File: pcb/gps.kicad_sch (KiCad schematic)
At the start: 7 parts, among them J10 RF_SMA, U18 MAX-M10S

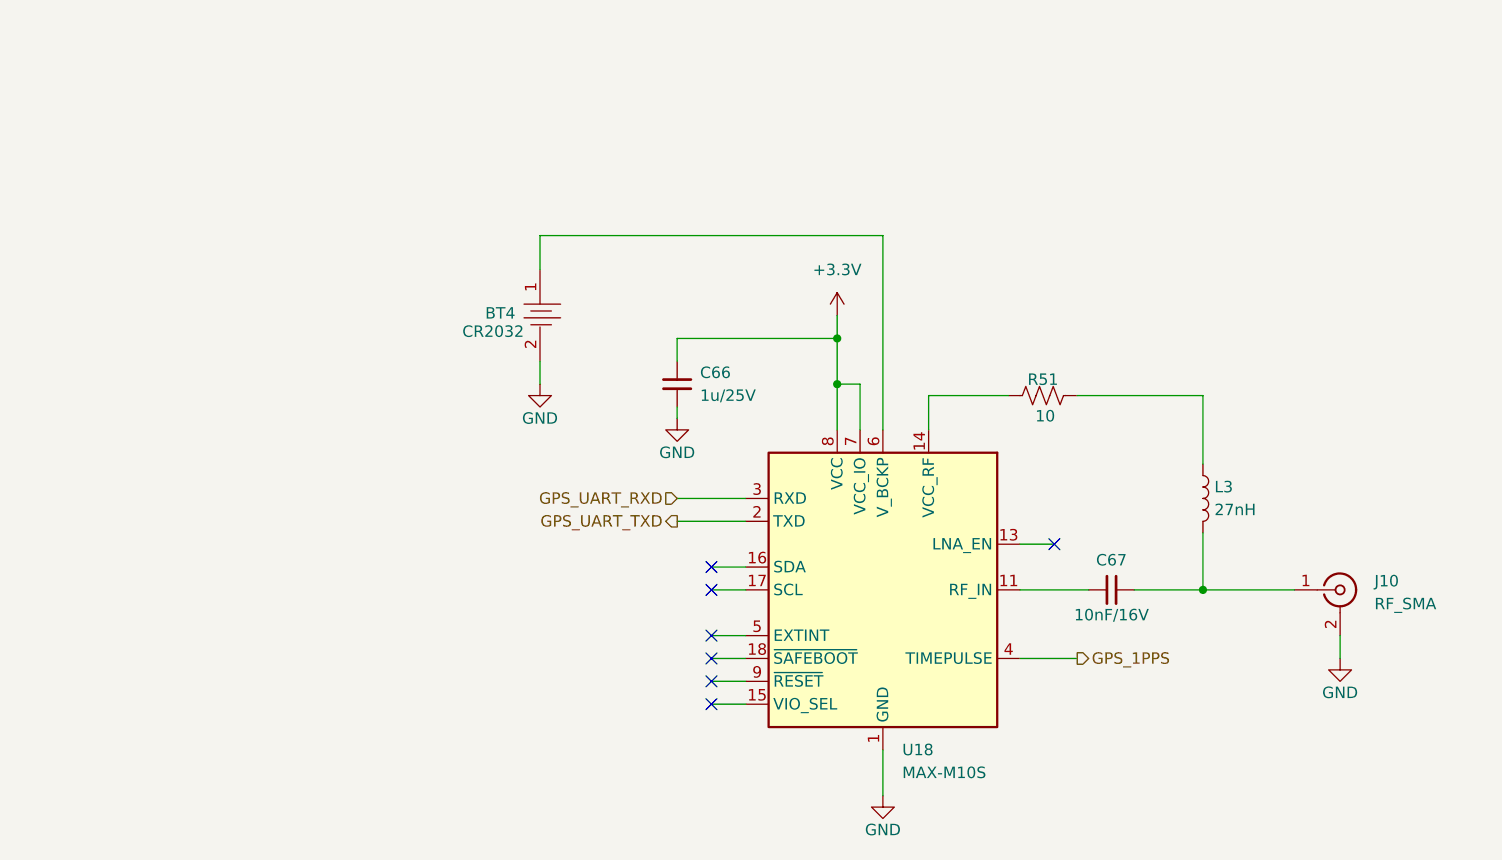
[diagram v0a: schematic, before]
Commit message: Wire GPS backup power network, import 4-layer stackup, add RF netclass
- gps.kicad_sch: CR2032/supercap backup network for V_BCKP (D6/D11/D12
  BAS116LT1G diodes, R52 10R charge resistor, C68 EDC474Z5R5V
  supercap), net labels GPS_RF_ANT/GPS_RF_IN on the antenna trace.
- foxhunt1.kicad_pcb: real JLCPCB 4-layer 1.6mm stackup imported
  (outer1oz/inner0.5oz, JLC04161H-7628/NOREQ construction).
- foxhunt1.kicad_pro: GPS_RF_50R netclass (2.75mm, sized for the prior
  2-layer board — needs updating to ~0.35mm once the 4-layer ground
  plane assignment is confirmed).

Co-Authored-By: Claude Sonnet 5 <noreply@anthropic.com>
Claude-Session: https://claude.ai/code/session_01LhLkuH6sQ5GbUZ61bG7p2h
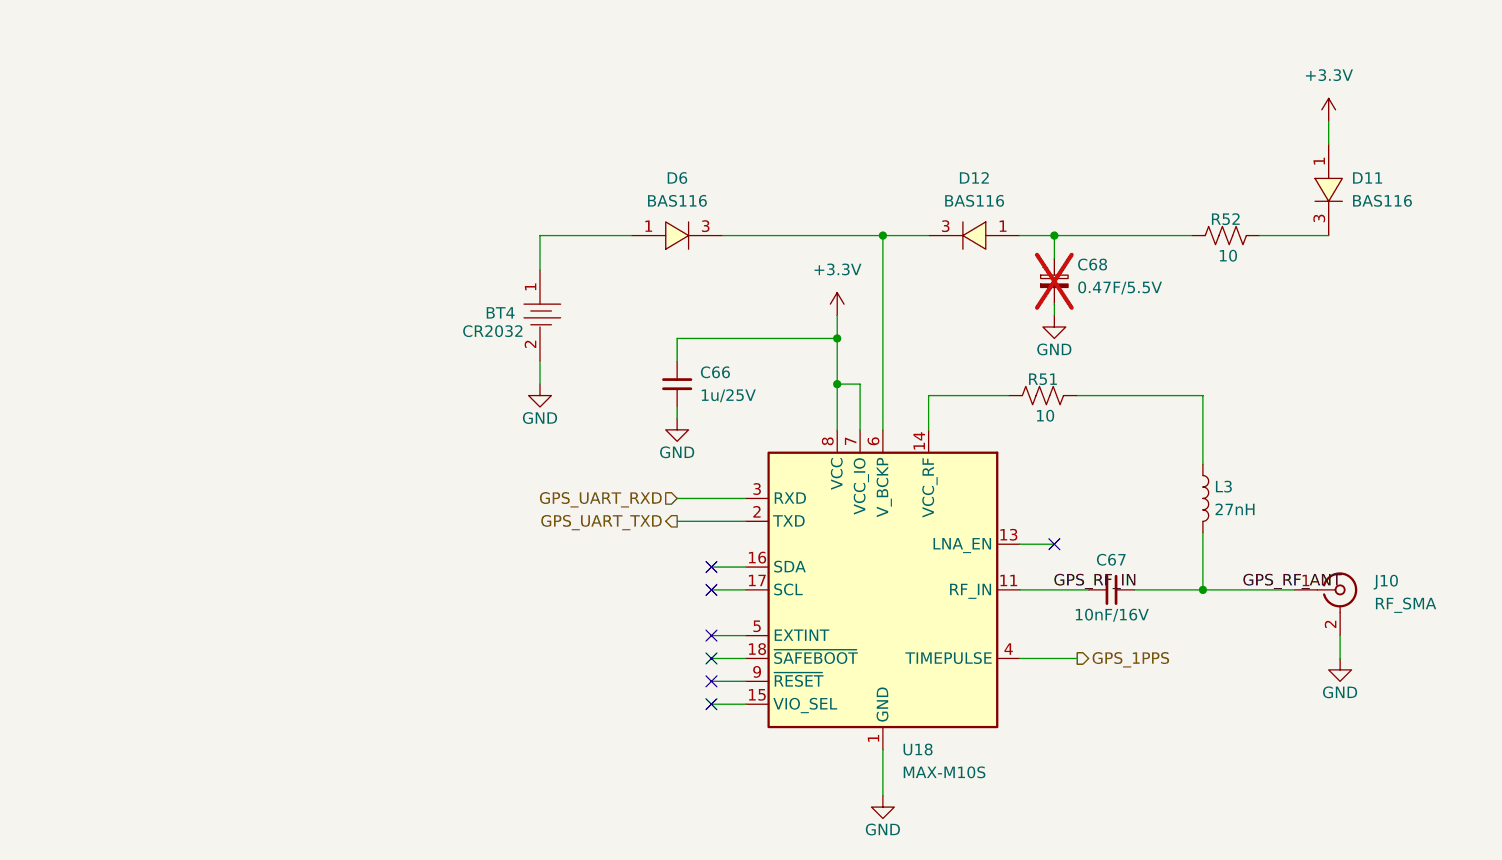
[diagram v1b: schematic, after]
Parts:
- added C68: 0.47F/5.5V, kicad_gx_library:CP_Supercap_EDC474Z5R5V_0.2x5mm, symbol Device:C_Polarized_Small
- added D11, D12, D6: BAS116, kicad_gx_library:SOT-23_L2.9-W1.3-P1.90-LS2.4-BR, symbol kicad_gx_library:BAS116LT1G
- added R52: 10, Resistor_SMD:R_0603_1608Metric, symbol Device:R_US
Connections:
- net +3.3V: now also D11.1
- net GND: now also C68.2
- net GPS_RF_IN: now reaches C67.1, U18.11 (RF_IN)
- net at U18.6 (V_BCKP): now also D12.3, D6.3; no longer BT4.1
- net GPS_RF_ANT: now reaches C67.2, J10.1 (In), L3.2
- new net: C68.1, D12.1, R52.2
- new net: BT4.1, D6.1
- new net: D11.3, R52.1

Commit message: Add SA818S-V sheet, update GPS antenna connector, MCU GPIO reassignments
- New SA818S-V sheet (U19): UART/PTT/MIC_IN wired; VBAT, ANT, PD, H/L
  still open (see sa818_pinout.md).
- gps.kicad_sch: J10 swapped to Amphenol 132289 edge-launch SMD SMA
  (same part planned for the SA818 antenna connector).
- mcu-esp32.kicad_sch: SA818 UART on IO6/IO7, PTT on IO16 (direct FET
  drive via Q10, not the originally-planned AND-gate scheme).
- peripherals.kicad_sch: in-progress PCA9555 channel changes.

Co-Authored-By: Claude Sonnet 5 <noreply@anthropic.com>
Claude-Session: https://claude.ai/code/session_01LhLkuH6sQ5GbUZ61bG7p2h
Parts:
- J10: footprint Connector_Coaxial:SMA_Amphenol_132134_Vertical -> Connector_Coaxial:SMA_Amphenol_132289_EdgeMount; LCSC Part # C3174425 -> C3172723; MPN 132134 -> 132289
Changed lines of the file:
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@@
 	(paper "A4")
+	(junction
+		(at 137.16 49.53)
+		(diameter 0)
+		(color 0 0 0 0)
+	)
 	(junction
 		(at 181.61 88.9)
@@
 	(wire
 		(pts
-			(xy 146.05 49.53) (xy 128.27 49.53)
+			(xy 146.05 49.53) (xy 137.16 49.53)
 		)
 		(stroke
@@
 		(pts
 			(xy 195.58 36.83) (xy 195.58 39.37)
+		)
+		(stroke
+			(width 0)
+			(type default)
+		)
+	)
+	(wire
+		(pts
+			(xy 137.16 49.53) (xy 128.27 49.53)
 		)
 		(stroke
@@
 	)
 	(symbol
+		(lib_id "power:PWR_FLAG")
+		(at 137.16 49.53 0)
+		(unit 1)
+		(body_style 1)
+		(exclude_from_sim no)
+		(in_bom yes)
+		(on_board yes)
+		(in_pos_files yes)
+		(dnp no)
+		(fields_autoplaced yes)
+		(property "Reference" "#FLG022"
+			(at 137.16 47.625 0)
+			(hide yes)
+			(show_name no)
+			(do_not_autoplace no)
+			(effects
+				(font
+					(size 1.27 1.27)
+				)
+			)
+		)
+		(property "Value" "PWR_FLAG"
+			(at 137.16 44.45 0)
+			(show_name no)
+			(do_not_autoplace no)
+			(effects
+				(font
+					(size 1.27 1.27)
+				)
+			)
+		)
+		(property "Footprint" ""
+			(at 137.16 49.53 0)
+			(hide yes)
+			(show_name no)
+			(do_not_autoplace no)
+			(effects
+				(font
+					(size 1.27 1.27)
+				)
+			)
+		)
+		(property "Datasheet" ""
+			(at 137.16 49.53 0)
+			(hide yes)
+			(show_name no)
+			(do_not_autoplace no)
+			(effects
+				(font
+					(size 1.27 1.27)
+				)
+			)
+		)
+		(property "Description" "Special symbol for telling ERC where power comes from"
+			(at 137.16 49.53 0)
+			(hide yes)
+			(show_name no)
+			(do_not_autoplace no)
+			(effects
+				(font
+					(size 1.27 1.27)
+				)
+			)
+		)
+		(pin "1"
+		)
+		(instances
+			(project "foxhunt1"
+				(path "/8399ba4b-9428-480d-8b65-76cf154b97a5/0c171942-64eb-4f5d-b37e-356ed65ec40c"
+					(reference "#FLG022")
+					(unit 1)
+				)
+			)
+		)
+	)
+	(symbol
 		(lib_id "kicad_gx_library:BAS116LT1G")
 		(at 156.21 49.53 180)
@@
 			)
 		)
-		(property "Footprint" "Connector_Coaxial:SMA_Amphenol_132134_Vertical"
+		(property "Footprint" "Connector_Coaxial:SMA_Amphenol_132289_EdgeMount"
 			(at 196.85 88.9 0)
 			(hide yes)
@@
 			)
 		)
-		(property "MPN" "132134"
+		(property "MPN" "132289"
 			(at 196.85 88.9 0)
 			(hide yes)
@@
 			)
 		)
-		(property "LCSC Part #" "C3174425"
+		(property "LCSC Part #" "C3172723"
 			(at 196.85 88.9 0)
 			(hide yes)

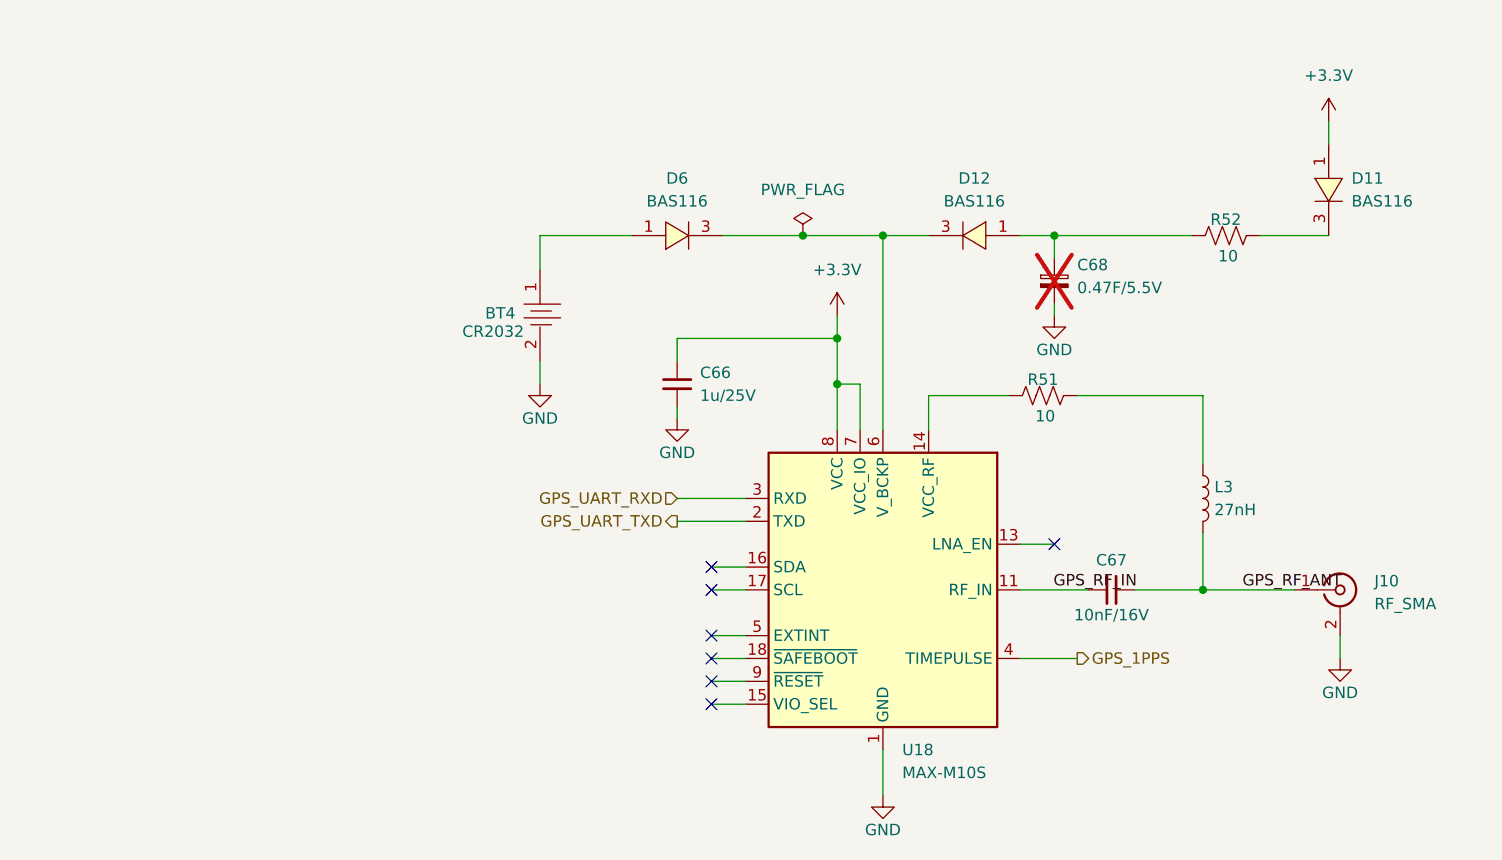
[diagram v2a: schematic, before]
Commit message: Wire SA818 PD/H-L and PTT opto, GPS power gating with bench bypass, RF detector groundwork
- SA818S-V: wire PD/H-L to PCA9555 expander outputs; swap PTT-keying FET
  for PC817 optocoupler isolation on the shared SA818S/external-HT PTT line
- GPS: add Q10 (AO3407A) high-side P-FET gating VCC+VCC_IO together for
  genuine hardware backup mode, driven via Q13 level-shifter from a new
  PCA9555 output (PERIPH_OUT_GPS_PWRON); add JP28 as a source-to-drain
  bench bypass across Q10 for unconditional power during bring-up; wire
  EXTINT to another PCA9555 output (PERIPH_OUT_GPS_EXTINT, pulled low by
  R57) to experiment with UART software-standby + external wake
- peripherals: reassign PCA9555 channels for the above plus SA818 PD/H-L
- audio/mcu-esp32: forward-power detector tap wiring groundwork
- docs: add vhf_matching_detector.md (matching network + RF detector BOM
  and layout), index it in _docs/README.md

Co-Authored-By: Claude Sonnet 5 <noreply@anthropic.com>
Claude-Session: https://claude.ai/code/session_01LhLkuH6sQ5GbUZ61bG7p2h
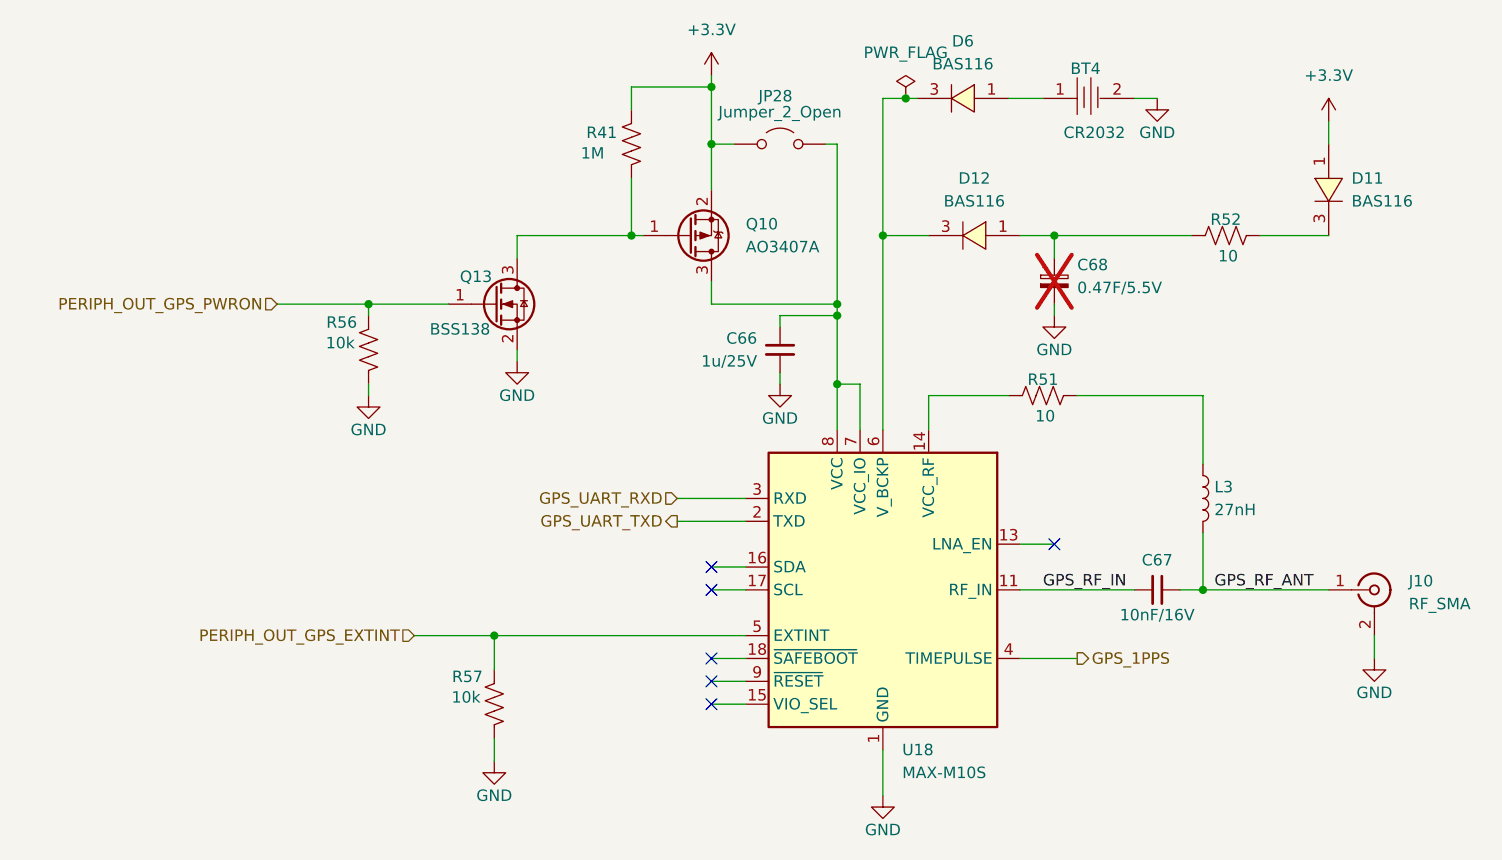
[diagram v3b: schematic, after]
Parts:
- added JP28: Jumper_2_Open, TestPoint:TestPoint_2Pads_Pitch2.54mm_Drill0.8mm, symbol Jumper:Jumper_2_Open
- added Q10: AO3407A, Package_TO_SOT_SMD:SOT-23, symbol Transistor_FET:AO3401A
- added Q13: BSS138, Package_TO_SOT_SMD:SOT-23, symbol Transistor_FET:BSS138
- added R41: 1M, Resistor_SMD:R_0603_1608Metric, symbol Device:R_US
- added R56, R57: 10k, Resistor_SMD:R_0603_1608Metric, symbol Device:R_US
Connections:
- net +3.3V: now also JP28.1 (A), Q10.2 (S), R41.2; no longer C66.1, U18.7 (VCC_IO), U18.8 (VCC)
- net GND: now also Q13.2 (S), R56.1, R57.1
- net PERIPH_OUT_GPS_EXTINT: now reaches U18.5 (EXTINT)
- net PERIPH_OUT_GPS_EXTINT: now also R57.2
- new net: C66.1, JP28.2 (B), Q10.3 (D), U18.7 (VCC_IO), U18.8 (VCC)
- new net: Q10.1 (G), Q13.3 (D), R41.1
- new net PERIPH_OUT_GPS_PWRON: Q13.1 (G), R56.2
- no-connect marks 7 -> 6
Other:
- moved on the sheet: BT4, C66, C67, D6, J10
